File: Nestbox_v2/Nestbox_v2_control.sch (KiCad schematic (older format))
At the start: 27 parts, among them CON301 Micro_SD_Card, P301 RX/TX, P302 TST/RST, SW301 SMD-BUTTON_2P-3.0X2.5X1.2+0.4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, U301 MSP430FR5969, Y301 Crystal

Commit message: added power footprints, final connector footprints
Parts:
- C301, C304, C305, C306, C307, C308: footprint (none) -> Capacitors_SMD:C_0603
- C302, C303: footprint SeeedOPL-Capacitor-2016:C0603 -> Capacitors_SMD:C_0603
- CON301: footprint (none) -> SeeedOPL-Connector-2016:MICRO-SD9+4P-SMD-16.1X14.5X1.85MM
- JP301: footprint (none) -> Pin_Headers:Pin_Header_Straight_1x02
- P301, P302: footprint Socket_Strips:Socket_Strip_Straight_1x02 -> Socket_Strips:Socket_Strip_Straight_1x02_Pitch2.54mm
- R301: footprint SeeedOPL-Resistor-2016:R0603 -> Resistors_SMD:R_0603
- R302, R303, R304, R305, R306, R307, R308, R309: footprint (none) -> Resistors_SMD:R_0603
- SW301: footprint SeeedOPL-Switch-2016:SW2-2.6-3.0X2.5X1.2+0.4MM -> Buttons_Switches_SMD:SW_SPST_B3S-1000
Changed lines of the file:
@@
 $EndComp
 $Comp
-L GND #PWR020
+L GND #PWR021
 U 1 1 586416A7
 P 6150 3750
-F 0 "#PWR020" H 6150 3500 50  0001 C CNN
+F 0 "#PWR021" H 6150 3500 50  0001 C CNN
 F 1 "GND" H 6150 3600 50  0000 C CNN
 F 2 "" H 6150 3750 50  0000 C CNN
@@
 $EndComp
 $Comp
-L +3.3V #PWR021
+L +3.3V #PWR022
 U 1 1 586418DC
 P 4300 1900
-F 0 "#PWR021" H 4300 1750 50  0001 C CNN
+F 0 "#PWR022" H 4300 1750 50  0001 C CNN
 F 1 "+3.3V" H 4300 2040 50  0000 C CNN
 F 2 "" H 4300 1900 50  0000 C CNN
@@
 $EndComp
 $Comp
-L GND #PWR022
+L GND #PWR023
 U 1 1 58641ADD
 P 2500 2250
-F 0 "#PWR022" H 2500 2000 50  0001 C CNN
+F 0 "#PWR023" H 2500 2000 50  0001 C CNN
 F 1 "GND" H 2500 2100 50  0000 C CNN
 F 2 "" H 2500 2250 50  0000 C CNN
@@
 $EndComp
 $Comp
-L +3.3V #PWR023
+L +3.3V #PWR024
 U 1 1 58641B00
 P 2850 1700
-F 0 "#PWR023" H 2850 1550 50  0001 C CNN
+F 0 "#PWR024" H 2850 1550 50  0001 C CNN
 F 1 "+3.3V" H 2850 1840 50  0000 C CNN
 F 2 "" H 2850 1700 50  0000 C CNN
@@
 $EndComp
 $Comp
-L GND #PWR024
+L GND #PWR025
 U 1 1 58652F3A
 P 4700 2450
-F 0 "#PWR024" H 4700 2200 50  0001 C CNN
+F 0 "#PWR025" H 4700 2200 50  0001 C CNN
 F 1 "GND" H 4700 2300 50  0000 C CNN
 F 2 "" H 4700 2450 50  0000 C CNN
@@
 $EndComp
 $Comp
-L GND #PWR025
+L GND #PWR026
 U 1 1 5865358A
 P 3400 1600
-F 0 "#PWR025" H 3400 1350 50  0001 C CNN
+F 0 "#PWR026" H 3400 1350 50  0001 C CNN
 F 1 "GND" H 3400 1450 50  0000 C CNN
 F 2 "" H 3400 1600 50  0000 C CNN
@@
 F 0 "P302" H 4400 7050 50  0000 C CNN
 F 1 "TST/RST" V 4500 6900 50  0000 C CNN
-F 2 "Socket_Strips:Socket_Strip_Straight_1x02" H 4400 6900 50  0001 C CNN
+F 2 "Socket_Strips:Socket_Strip_Straight_1x02_Pitch2.54mm" H 4400 6900 50  0001 C CNN
 F 3 "" H 4400 6900 50  0000 C CNN
 F 4 "" H 4400 6900 50  0001 C CNN "MPN"
@@
 $EndComp
 $Comp
-L GNDA #PWR026
+L GNDA #PWR027
 U 1 1 587B6902
 P 3300 2400
-F 0 "#PWR026" H 3300 2150 50  0001 C CNN
+F 0 "#PWR027" H 3300 2150 50  0001 C CNN
 F 1 "GNDA" H 3300 2250 50  0000 C CNN
 F 2 "" H 3300 2400 50  0000 C CNN
@@
 $EndComp
 $Comp
-L GNDA #PWR027
+L GNDA #PWR028
 U 1 1 587B69F1
 P 3600 2400
-F 0 "#PWR027" H 3600 2150 50  0001 C CNN
+F 0 "#PWR028" H 3600 2150 50  0001 C CNN
 F 1 "GNDA" H 3600 2250 50  0000 C CNN
 F 2 "" H 3600 2400 50  0000 C CNN
@@
 $EndComp
 $Comp
-L GNDA #PWR028
+L GNDA #PWR029
 U 1 1 587B6A2F
 P 3900 2400
-F 0 "#PWR028" H 3900 2150 50  0001 C CNN
+F 0 "#PWR029" H 3900 2150 50  0001 C CNN
 F 1 "GNDA" H 3900 2250 50  0000 C CNN
 F 2 "" H 3900 2400 50  0000 C CNN
@@
 F 0 "SW301" H 9700 4950 45  0000 L BNN
 F 1 "SMD-BUTTON_2P-3.0X2.5X1.2+0.4MM_" H 10050 4950 45  0000 L BNN
-F 2 "SeeedOPL-Switch-2016:SW2-2.6-3.0X2.5X1.2+0.4MM" H 10000 4900 60  0001 C CNN
+F 2 "Buttons_Switches_SMD:SW_SPST_B3S-1000" H 10000 4900 60  0001 C CNN
 F 3 "" H 10000 4900 60  0001 C CNN
 F 4 "B3U-1000P-B" H 10030 5050 20  0001 C CNN "MPN"
@@
 $EndComp
 $Comp
-L GND #PWR029
+L GND #PWR030
 U 1 1 587B96DD
 P 10000 5300
-F 0 "#PWR029" H 10000 5050 50  0001 C CNN
+F 0 "#PWR030" H 10000 5050 50  0001 C CNN
 F 1 "GND" H 10000 5150 50  0000 C CNN
 F 2 "" H 10000 5300 50  0000 C CNN
@@
 $EndComp
 $Comp
-L +3.3V #PWR030
+L +3.3V #PWR031
 U 1 1 587B9736
 P 10000 4100
-F 0 "#PWR030" H 10000 3950 50  0001 C CNN
+F 0 "#PWR031" H 10000 3950 50  0001 C CNN
 F 1 "+3.3V" H 10000 4240 50  0000 C CNN
 F 2 "" H 10000 4100 50  0000 C CNN
@@
 $EndComp
 $Comp
-L GND #PWR031
+L GND #PWR032
 U 1 1 587B97E4
 P 9600 5400
-F 0 "#PWR031" H 9600 5150 50  0001 C CNN
+F 0 "#PWR032" H 9600 5150 50  0001 C CNN
 F 1 "GND" H 9600 5250 50  0000 C CNN
 F 2 "" H 9600 5400 50  0000 C CNN
@@
 $EndComp
 $Comp
-L GND #PWR032
+L GND #PWR033
 U 1 1 587B9834
 P 9300 5400
-F 0 "#PWR032" H 9300 5150 50  0001 C CNN
+F 0 "#PWR033" H 9300 5150 50  0001 C CNN
 F 1 "GND" H 9300 5250 50  0000 C CNN
 F 2 "" H 9300 5400 50  0000 C CNN
@@
 F 0 "P301" H 3950 7750 50  0000 C CNN
 F 1 "RX/TX" V 4050 7600 50  0000 C CNN
-F 2 "Socket_Strips:Socket_Strip_Straight_1x02" H 3950 7600 50  0001 C CNN
+F 2 "Socket_Strips:Socket_Strip_Straight_1x02_Pitch2.54mm" H 3950 7600 50  0001 C CNN
 F 3 "" H 3950 7600 50  0000 C CNN
 F 4 "" H 3950 7600 50  0001 C CNN "MPN"
@@
 F 0 "C303" H 3500 1850 45  0000 L BNN
 F 1 "25 pF" H 3500 1700 45  0000 L BNN
-F 2 "SeeedOPL-Capacitor-2016:C0603" H 3650 1800 60  0001 C CNN
+F 2 "Capacitors_SMD:C_0603" H 3650 1800 60  0001 C CNN
 F 3 "" H 3650 1800 60  0001 C CNN
 F 4 "CC0603JRNPO9BN120" H 3680 1950 20  0001 C CNN "MPN"
@@
 F 0 "C302" H 3050 1850 45  0000 L BNN
 F 1 "25 pF" H 3050 1700 45  0000 L BNN
-F 2 "SeeedOPL-Capacitor-2016:C0603" H 3200 1800 60  0001 C CNN
+F 2 "Capacitors_SMD:C_0603" H 3200 1800 60  0001 C CNN
 F 3 "" H 3200 1800 60  0001 C CNN
 F 4 "CC0603JRNPO9BN120" H 3230 1950 20  0001 C CNN "MPN"
@@
 	9300 4950 9300 5050
 $Comp
-L GND #PWR033
+L GND #PWR034
 U 1 1 587D2523
 P 2450 2450
-F 0 "#PWR033" H 2450 2200 50  0001 C CNN
+F 0 "#PWR034" H 2450 2200 50  0001 C CNN
 F 1 "GND" H 2450 2300 50  0000 C CNN
 F 2 "" H 2450 2450 50  0000 C CNN
@@
 	4350 6650 4350 6700
 $Comp
-L +3.3V #PWR034
+L +3.3V #PWR035
 U 1 1 58BC4BB7
 P 4850 6600
-F 0 "#PWR034" H 4850 6450 50  0001 C CNN
+F 0 "#PWR035" H 4850 6450 50  0001 C CNN
 F 1 "+3.3V" H 4850 6740 50  0000 C CNN
 F 2 "" H 4850 6600 50  0000 C CNN
@@
 F 0 "R301" H 4500 6650 45  0000 L BNN
 F 1 "47K" H 4500 6500 45  0000 L BNN
-F 2 "SeeedOPL-Resistor-2016:R0603" H 4650 6600 40  0001 C CNN
+F 2 "Resistors_SMD:R_0603" H 4650 6600 40  0001 C CNN
 F 3 "" H 4650 6600 40  0001 C CNN
 F 4 "FHCFR-1_4W-473J" H 4680 6750 20  0001 C CNN "MPN"
@@
 	10200 4850 10200 4900
 $Comp
-L GND #PWR035
+L GND #PWR036
 U 1 1 58BF19D6
 P 10200 5300
-F 0 "#PWR035" H 10200 5050 50  0001 C CNN
+F 0 "#PWR036" H 10200 5050 50  0001 C CNN
 F 1 "GND" H 10200 5150 50  0000 C CNN
 F 2 "" H 10200 5300 50  0000 C CNN
@@
 F 0 "CON301" H 9750 2367 50  0000 C CNN
 F 1 "Micro_SD_Card" H 9750 2276 50  0000 C CNN
-F 2 "" H 10950 1950 50  0000 C CNN
+F 2 "SeeedOPL-Connector-2016:MICRO-SD9+4P-SMD-16.1X14.5X1.85MM" H 10950 1950 50  0001 C CNN
 F 3 "" H 9800 1650 50  0000 C CNN
 	1    9800 1650
@@
 SPI_MOSI
 $Comp
-L +3.3V #PWR036
+L +3.3V #PWR037
 U 1 1 59FCECA7
 P 6500 1600
-F 0 "#PWR036" H 6500 1450 50  0001 C CNN
+F 0 "#PWR037" H 6500 1450 50  0001 C CNN
 F 1 "+3.3V" H 6500 1740 50  0000 C CNN
 F 2 "" H 6500 1600 50  0000 C CNN
@@
 $EndComp
 $Comp
-L GND #PWR037
+L GND #PWR038
 U 1 1 59FCED84
 P 7000 1900
-F 0 "#PWR037" H 7000 1650 50  0001 C CNN
+F 0 "#PWR038" H 7000 1650 50  0001 C CNN
 F 1 "GND" H 7000 1750 50  0000 C CNN
 F 2 "" H 7000 1900 50  0000 C CNN
@@
 F 0 "C306" H 7218 1796 50  0000 L CNN
 F 1 "100u" H 7218 1705 50  0000 L CNN
-F 2 "" H 7138 1600 50  0000 C CNN
+F 2 "Capacitors_SMD:C_0603" H 7138 1600 50  0001 C CNN
 F 3 "" H 7100 1750 50  0000 C CNN
 F 4 "667-ECE-A0JKA101" H 7100 1750 60  0001 C CNN "Mouser-Part"
@@
 F 0 "C307" H 7615 1796 50  0000 L CNN
 F 1 "0.1u" H 7615 1705 50  0000 L CNN
-F 2 "" H 7538 1600 50  0000 C CNN
+F 2 "Capacitors_SMD:C_0603" H 7538 1600 50  0001 C CNN
 F 3 "" H 7500 1750 50  0000 C CNN
 	1    7500 1750
@@
 F 0 "R302" V 6543 1600 50  0000 C CNN
 F 1 "0E" V 6634 1600 50  0000 C CNN
-F 2 "" V 6680 1600 50  0000 C CNN
+F 2 "Resistors_SMD:R_0603" V 6680 1600 50  0001 C CNN
 F 3 "" H 6750 1600 50  0000 C CNN
 	1    6750 1600
@@
 F 0 "R306" H 9370 5246 50  0000 L CNN
 F 1 "1K" H 9370 5155 50  0000 L CNN
-F 2 "" V 9230 5200 50  0000 C CNN
+F 2 "Resistors_SMD:R_0603" V 9230 5200 50  0001 C CNN
 F 3 "" H 9300 5200 50  0000 C CNN
 	1    9300 5200
@@
 F 0 "R307" H 9670 5246 50  0000 L CNN
 F 1 "1K" H 9670 5155 50  0000 L CNN
-F 2 "" V 9530 5200 50  0000 C CNN
+F 2 "Resistors_SMD:R_0603" V 9530 5200 50  0001 C CNN
 F 3 "" H 9600 5200 50  0000 C CNN
 	1    9600 5200
@@
 F 0 "R309" H 10270 4746 50  0000 L CNN
 F 1 "10K" H 10270 4655 50  0000 L CNN
-F 2 "" V 10130 4700 50  0000 C CNN
+F 2 "Resistors_SMD:R_0603" V 10130 4700 50  0001 C CNN
 F 3 "" H 10200 4700 50  0000 C CNN
 	1    10200 4700
@@
 F 0 "R308" H 10070 4396 50  0000 L CNN
 F 1 "10K" H 10070 4305 50  0000 L CNN
-F 2 "" V 9930 4350 50  0000 C CNN
+F 2 "Resistors_SMD:R_0603" V 9930 4350 50  0001 C CNN
 F 3 "" H 10000 4350 50  0000 C CNN
 	1    10000 4350
@@
 F 0 "C308" H 10315 5096 50  0000 L CNN
 F 1 "100n" H 10315 5005 50  0000 L CNN
-F 2 "" H 10238 4900 50  0000 C CNN
+F 2 "Capacitors_SMD:C_0603" H 10238 4900 50  0001 C CNN
 F 3 "" H 10200 5050 50  0000 C CNN
 	1    10200 5050
@@
 F 0 "C304" V 4248 2000 50  0000 C CNN
 F 1 "10u" V 4339 2000 50  0000 C CNN
-F 2 "" H 4538 1850 50  0000 C CNN
+F 2 "Capacitors_SMD:C_0603" H 4538 1850 50  0001 C CNN
 F 3 "" H 4500 2000 50  0000 C CNN
 	1    4500 2000
@@
 F 0 "C305" V 4248 2400 50  0000 C CNN
 F 1 "100n" V 4339 2400 50  0000 C CNN
-F 2 "" H 4538 2250 50  0000 C CNN
+F 2 "Capacitors_SMD:C_0603" H 4538 2250 50  0001 C CNN
 F 3 "" H 4500 2400 50  0000 C CNN
 	1    4500 2400
@@
 F 0 "C301" V 2398 2250 50  0000 C CNN
 F 1 "100n" V 2489 2250 50  0000 C CNN
-F 2 "" H 2688 2100 50  0000 C CNN
+F 2 "Capacitors_SMD:C_0603" H 2688 2100 50  0001 C CNN
 F 3 "" H 2650 2250 50  0000 C CNN
 	1    2650 2250
@@
 F 0 "JP301" H 4400 7614 50  0000 C CNN
 F 1 "Jumper" H 4400 7523 50  0000 C CNN
-F 2 "" H 4400 7350 50  0001 C CNN
+F 2 "Pin_Headers:Pin_Header_Straight_1x02" H 4400 7350 50  0001 C CNN
 F 3 "" H 4400 7350 50  0001 C CNN
 	1    4400 7350
@@
 F 0 "R303" V 8550 1750 50  0000 C CNN
 F 1 "47R" V 8600 1550 50  0000 C CNN
-F 2 "" V 8530 1550 50  0000 C CNN
+F 2 "Resistors_SMD:R_0603" V 8530 1550 50  0001 C CNN
 F 3 "" H 8600 1550 50  0000 C CNN
 	1    8600 1550
@@
 F 0 "R304" V 8550 1950 50  0000 C CNN
 F 1 "47R" V 8600 1750 50  0000 C CNN
-F 2 "" V 8530 1750 50  0000 C CNN
+F 2 "Resistors_SMD:R_0603" V 8530 1750 50  0001 C CNN
 F 3 "" H 8600 1750 50  0000 C CNN
 	1    8600 1750
@@
 F 0 "R305" V 8550 2150 50  0000 C CNN
 F 1 "47R" V 8600 1950 50  0000 C CNN
-F 2 "" V 8530 1950 50  0000 C CNN
+F 2 "Resistors_SMD:R_0603" V 8530 1950 50  0001 C CNN
 F 3 "" H 8600 1950 50  0000 C CNN
 	1    8600 1950

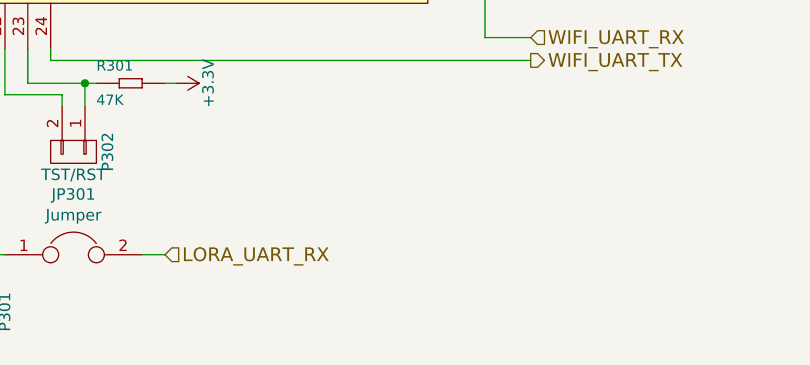
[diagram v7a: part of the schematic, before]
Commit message: correct size of the PCB drawn with connector arrangement done as well
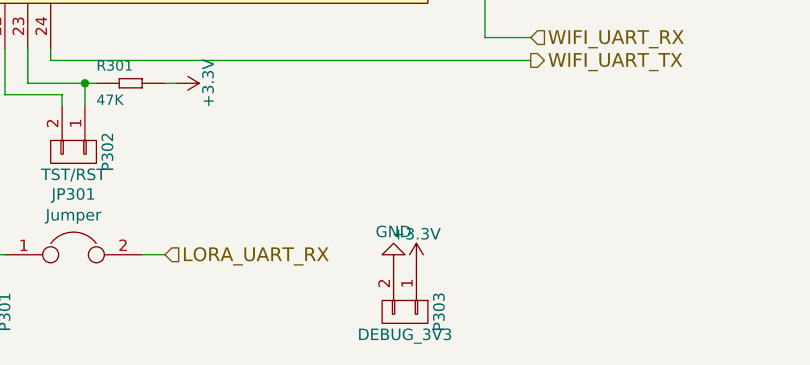
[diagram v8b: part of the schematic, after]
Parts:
- added P303: DEBUG_3V3, Socket_Strips:Socket_Strip_Straight_1x02_Pitch2.54mm, symbol CONN_01X02
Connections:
- net +3V3: now also P303.1 (P1)
- net GND: now also P303.2 (P2)
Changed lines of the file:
@@
 $EndComp
 $Comp
-L GND #PWR021
+L GND #PWR313
 U 1 1 586416A7
 P 6150 3750
-F 0 "#PWR021" H 6150 3500 50  0001 C CNN
+F 0 "#PWR313" H 6150 3500 50  0001 C CNN
 F 1 "GND" H 6150 3600 50  0000 C CNN
 F 2 "" H 6150 3750 50  0000 C CNN
@@
 $EndComp
 $Comp
-L +3.3V #PWR022
+L +3.3V #PWR308
 U 1 1 586418DC
 P 4300 1900
-F 0 "#PWR022" H 4300 1750 50  0001 C CNN
+F 0 "#PWR308" H 4300 1750 50  0001 C CNN
 F 1 "+3.3V" H 4300 2040 50  0000 C CNN
 F 2 "" H 4300 1900 50  0000 C CNN
@@
 $EndComp
 $Comp
-L GND #PWR023
+L GND #PWR302
 U 1 1 58641ADD
 P 2500 2250
-F 0 "#PWR023" H 2500 2000 50  0001 C CNN
+F 0 "#PWR302" H 2500 2000 50  0001 C CNN
 F 1 "GND" H 2500 2100 50  0000 C CNN
 F 2 "" H 2500 2250 50  0000 C CNN
@@
 $EndComp
 $Comp
-L +3.3V #PWR024
+L +3.3V #PWR303
 U 1 1 58641B00
 P 2850 1700
-F 0 "#PWR024" H 2850 1550 50  0001 C CNN
+F 0 "#PWR303" H 2850 1550 50  0001 C CNN
 F 1 "+3.3V" H 2850 1840 50  0000 C CNN
 F 2 "" H 2850 1700 50  0000 C CNN
@@
 $EndComp
 $Comp
-L GND #PWR025
+L GND #PWR309
 U 1 1 58652F3A
 P 4700 2450
-F 0 "#PWR025" H 4700 2200 50  0001 C CNN
+F 0 "#PWR309" H 4700 2200 50  0001 C CNN
 F 1 "GND" H 4700 2300 50  0000 C CNN
 F 2 "" H 4700 2450 50  0000 C CNN
@@
 $EndComp
 $Comp
-L GND #PWR026
+L GND #PWR305
 U 1 1 5865358A
 P 3400 1600
-F 0 "#PWR026" H 3400 1350 50  0001 C CNN
+F 0 "#PWR305" H 3400 1350 50  0001 C CNN
 F 1 "GND" H 3400 1450 50  0000 C CNN
 F 2 "" H 3400 1600 50  0000 C CNN
@@
 $EndComp
 $Comp
-L GNDA #PWR027
+L GNDA #PWR304
 U 1 1 587B6902
 P 3300 2400
-F 0 "#PWR027" H 3300 2150 50  0001 C CNN
+F 0 "#PWR304" H 3300 2150 50  0001 C CNN
 F 1 "GNDA" H 3300 2250 50  0000 C CNN
 F 2 "" H 3300 2400 50  0000 C CNN
@@
 $EndComp
 $Comp
-L GNDA #PWR028
+L GNDA #PWR306
 U 1 1 587B69F1
 P 3600 2400
-F 0 "#PWR028" H 3600 2150 50  0001 C CNN
+F 0 "#PWR306" H 3600 2150 50  0001 C CNN
 F 1 "GNDA" H 3600 2250 50  0000 C CNN
 F 2 "" H 3600 2400 50  0000 C CNN
@@
 $EndComp
 $Comp
-L GNDA #PWR029
+L GNDA #PWR307
 U 1 1 587B6A2F
 P 3900 2400
-F 0 "#PWR029" H 3900 2150 50  0001 C CNN
+F 0 "#PWR307" H 3900 2150 50  0001 C CNN
 F 1 "GNDA" H 3900 2250 50  0000 C CNN
 F 2 "" H 3900 2400 50  0000 C CNN
@@
 $EndComp
 $Comp
-L GND #PWR030
+L GND #PWR319
 U 1 1 587B96DD
 P 10000 5300
-F 0 "#PWR030" H 10000 5050 50  0001 C CNN
+F 0 "#PWR319" H 10000 5050 50  0001 C CNN
 F 1 "GND" H 10000 5150 50  0000 C CNN
 F 2 "" H 10000 5300 50  0000 C CNN
@@
 $EndComp
 $Comp
-L +3.3V #PWR031
+L +3.3V #PWR318
 U 1 1 587B9736
 P 10000 4100
-F 0 "#PWR031" H 10000 3950 50  0001 C CNN
+F 0 "#PWR318" H 10000 3950 50  0001 C CNN
 F 1 "+3.3V" H 10000 4240 50  0000 C CNN
 F 2 "" H 10000 4100 50  0000 C CNN
@@
 $EndComp
 $Comp
-L GND #PWR032
+L GND #PWR317
 U 1 1 587B97E4
 P 9600 5400
-F 0 "#PWR032" H 9600 5150 50  0001 C CNN
+F 0 "#PWR317" H 9600 5150 50  0001 C CNN
 F 1 "GND" H 9600 5250 50  0000 C CNN
 F 2 "" H 9600 5400 50  0000 C CNN
@@
 $EndComp
 $Comp
-L GND #PWR033
+L GND #PWR316
 U 1 1 587B9834
 P 9300 5400
-F 0 "#PWR033" H 9300 5150 50  0001 C CNN
+F 0 "#PWR316" H 9300 5150 50  0001 C CNN
 F 1 "GND" H 9300 5250 50  0000 C CNN
 F 2 "" H 9300 5400 50  0000 C CNN
@@
 	9300 4950 9300 5050
 $Comp
-L GND #PWR034
+L GND #PWR301
 U 1 1 587D2523
 P 2450 2450
-F 0 "#PWR034" H 2450 2200 50  0001 C CNN
+F 0 "#PWR301" H 2450 2200 50  0001 C CNN
 F 1 "GND" H 2450 2300 50  0000 C CNN
 F 2 "" H 2450 2450 50  0000 C CNN
@@
 	4350 6650 4350 6700
 $Comp
-L +3.3V #PWR035
+L +3.3V #PWR310
 U 1 1 58BC4BB7
 P 4850 6600
-F 0 "#PWR035" H 4850 6450 50  0001 C CNN
+F 0 "#PWR310" H 4850 6450 50  0001 C CNN
 F 1 "+3.3V" H 4850 6740 50  0000 C CNN
 F 2 "" H 4850 6600 50  0000 C CNN
@@
 	10200 4850 10200 4900
 $Comp
-L GND #PWR036
+L GND #PWR320
 U 1 1 58BF19D6
 P 10200 5300
-F 0 "#PWR036" H 10200 5050 50  0001 C CNN
+F 0 "#PWR320" H 10200 5050 50  0001 C CNN
 F 1 "GND" H 10200 5150 50  0000 C CNN
 F 2 "" H 10200 5300 50  0000 C CNN
@@
 SPI_MOSI
 $Comp
-L +3.3V #PWR037
+L +3.3V #PWR314
 U 1 1 59FCECA7
 P 6500 1600
-F 0 "#PWR037" H 6500 1450 50  0001 C CNN
+F 0 "#PWR314" H 6500 1450 50  0001 C CNN
 F 1 "+3.3V" H 6500 1740 50  0000 C CNN
 F 2 "" H 6500 1600 50  0000 C CNN
@@
 $EndComp
 $Comp
-L GND #PWR038
+L GND #PWR315
 U 1 1 59FCED84
 P 7000 1900
-F 0 "#PWR038" H 7000 1650 50  0001 C CNN
+F 0 "#PWR315" H 7000 1650 50  0001 C CNN
 F 1 "GND" H 7000 1750 50  0000 C CNN
 F 2 "" H 7000 1900 50  0000 C CNN
@@
 Wire Wire Line
 	4200 2200 4200 2450
+$Comp
+L CONN_01X02 P303
+U 1 1 5B0C483C
+P 5850 7600
+F 0 "P303" H 5850 7750 50  0000 C CNN
+F 1 "DEBUG_3V3" V 5950 7600 50  0000 C CNN
+F 2 "Socket_Strips:Socket_Strip_Straight_1x02_Pitch2.54mm" H 5850 7600 50  0001 C CNN
+F 3 "" H 5850 7600 50  0000 C CNN
+	1    5850 7600
+	0    1    1    0
+$EndComp
+$Comp
+L +3.3V #PWR312
+U 1 1 5B0C49AB
+P 5900 7400
+F 0 "#PWR312" H 5900 7250 50  0001 C CNN
+F 1 "+3.3V" H 5900 7540 50  0000 C CNN
+F 2 "" H 5900 7400 50  0000 C CNN
+F 3 "" H 5900 7400 50  0000 C CNN
+	1    5900 7400
+	1    0    0    -1
+$EndComp
+$Comp
+L GND #PWR311
+U 1 1 5B0C4B76
+P 5800 7400
+F 0 "#PWR311" H 5800 7150 50  0001 C CNN
+F 1 "GND" H 5800 7250 50  0000 C CNN
+F 2 "" H 5800 7400 50  0000 C CNN
+F 3 "" H 5800 7400 50  0000 C CNN
+	1    5800 7400
+	-1   0    0    1
+$EndComp
 $EndSCHEMATC
